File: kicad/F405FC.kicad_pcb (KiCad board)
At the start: 4 copper layers, 36 x 36 mm, 161 parts, among them J1 USB4105-GF-A, J2 ESC, J3 HD VTX, J4 GPS, J5 ELRS, P1 VBAT, P10 LED_DIN, P11 5V, P12 GND, P13 5V, P14 BUZ_N, P15 UART5_TX, P16 UART5_RX, P17 UART6_TX, P18 UART6_RX, P19 MOTOR5, P2 GND, P20 MOTOR6, P21 MOTOR7, P22 MOTOR8, P23 RSSI_IN, P24 GND, P25 5V, P3 10V, P4 GND, P5 CAM1_VID, P6 CAM2_VID, P7 VTX_VID, P8 5V, P9 GND, Q1 PMV40UN2, Q2 NX7002AK, SW1 BOOT, U1 LMR38020FSDDAR, U10 W25N01GV, U11 TS5A3159A, U12 SN74LV1T125, U13 USBLC6-2SC6, U2 LMR38020FSDDAR, U3 STM32F405RGT6, U4 LP38692MP-3.3, U5 LP5907MFX-3.3, U6 ICM-42688-P, U7 BMI270, U8 BMP390, U9 IIS2MDC, Y1 8MHz

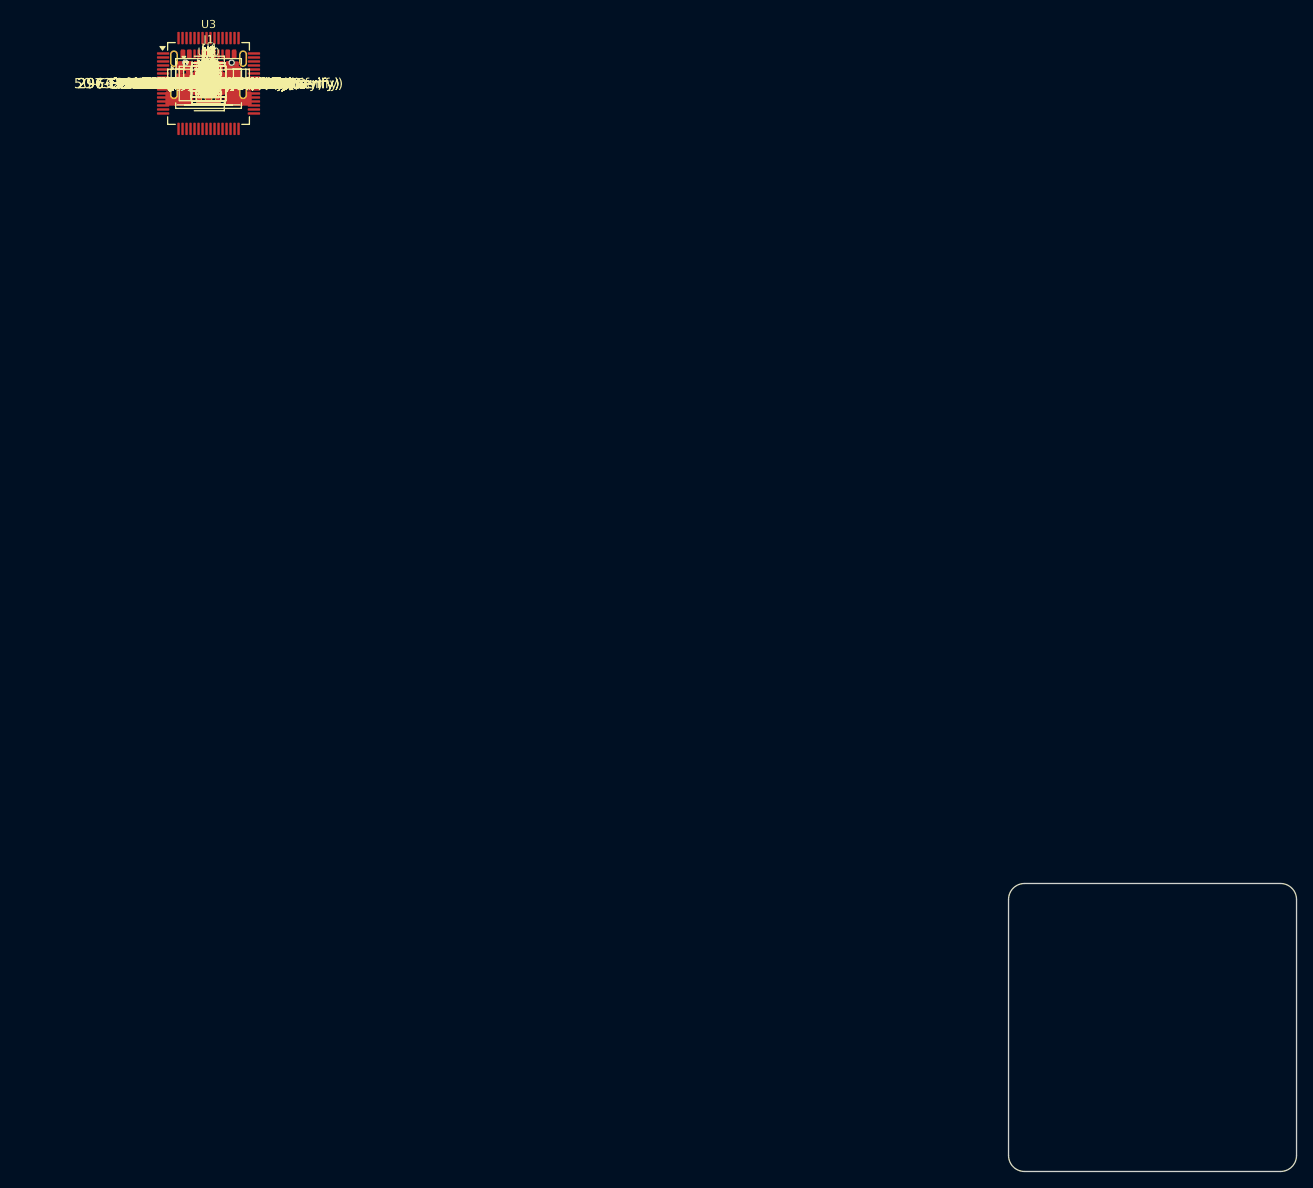
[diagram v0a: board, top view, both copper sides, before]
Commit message: Gate 1 fixes (crystal gm evidence, LDO output ESR, X7R caps, 50V HF cap, per-MPN datasheets, in_bom flags, project-file merge, parity fields), power re-audit fixes (board-level thermal envelope, USB inrush deviation, R41 VTX 0R link), PCB placement + legalizer + grommet keepouts; Gate 1 reports
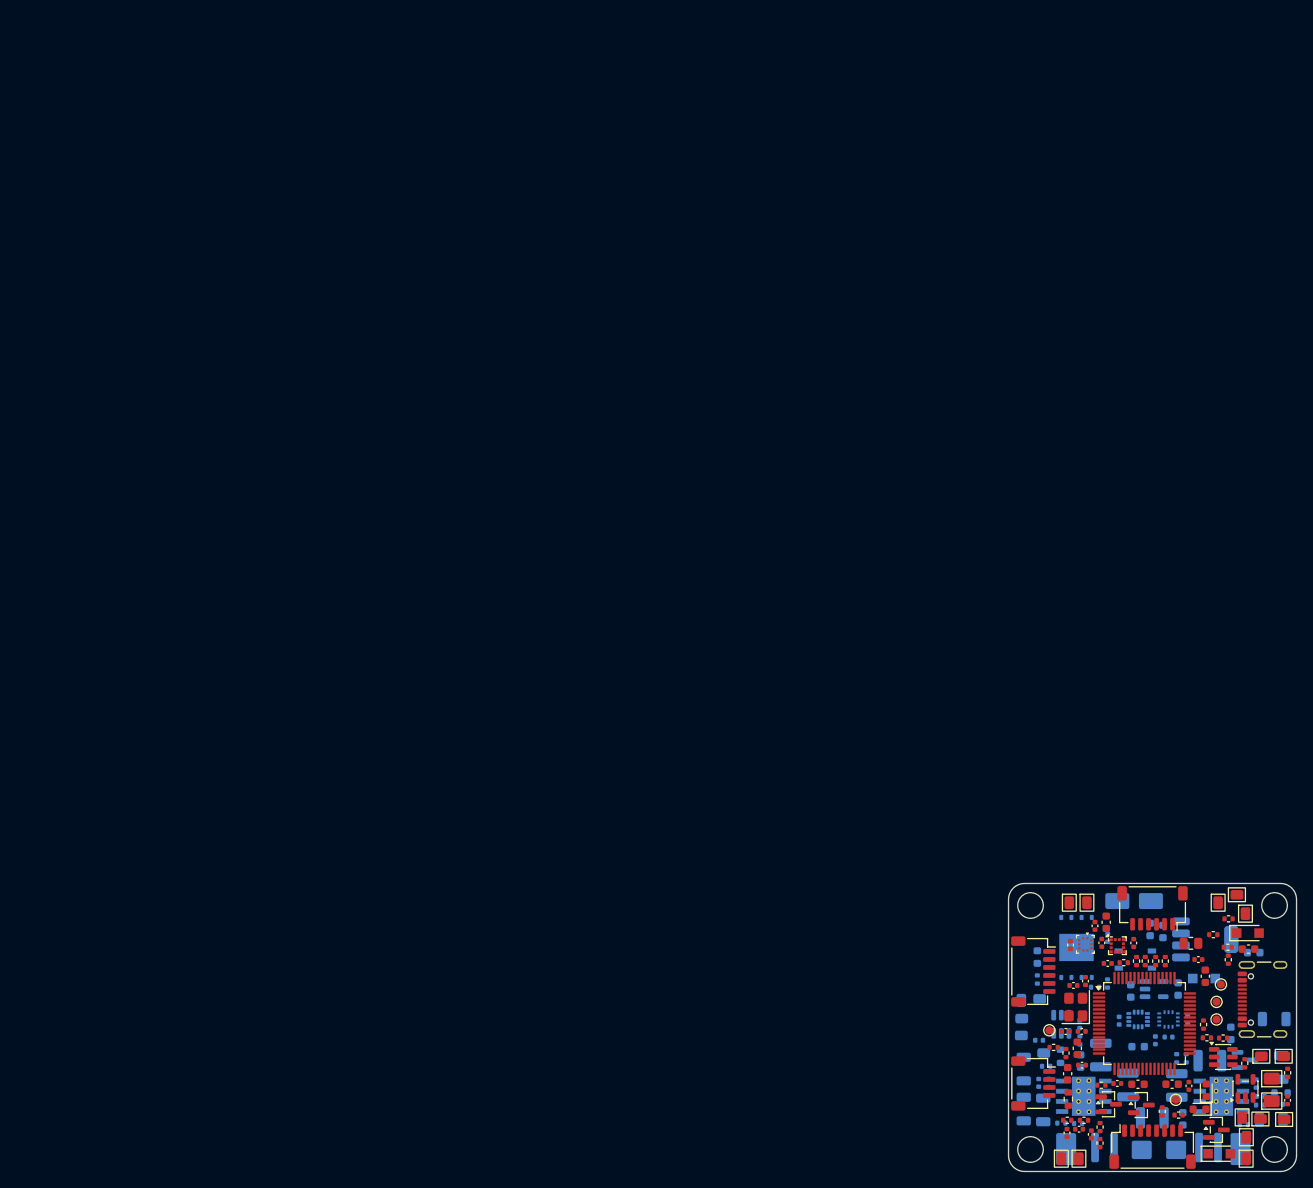
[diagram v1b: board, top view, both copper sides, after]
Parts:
- removed C21: 100nF X7R 16V, Capacitor_SMD:C_0402_1005Metric
- added R41: 0R 2A, Resistor_SMD:R_0805_2012Metric, F.Cu at (122.8, 107.5)
- C1, C10, C11, C12, C13, C14, C15, C16, C19, C2, C22, C3, C38, C4, C40, C41, C42, C48, C49, C5, C6, C7, C8, C9, D1, D10, D5, L1, L2, P1, P2, P3, P4, P5, P6, P7, P8, P9, Q2, R1, R10, R11, R12, R13, R2, R29, R3, R30, R31, R4, R5, R6, R7, R8, R9, SW1, U1, U10, U11, U2, U4, U5, U6, U7: moved to B.Cu
- C17: value 100nF X7R 16V -> 100nF X7R 100V; footprint Capacitor_SMD:C_0402_1005Metric -> Capacitor_SMD:C_0603_1608Metric; moved to B.Cu
- C18: value 4.7uF X5R 10V -> 4.7uF X5R 16V; moved to B.Cu
- C20: value 10uF X5R 25V -> 2.2uF X5R 16V; footprint Capacitor_SMD:C_0805_2012Metric -> Capacitor_SMD:C_0603_1608Metric; moved to B.Cu
- C23, C39: value 2.2uF X5R 16V -> 2.2uF X7R 16V; moved to B.Cu
- C29: value 4.7uF X5R 10V -> 4.7uF X5R 16V
- C47: value 1uF X5R 25V -> 4.7uF X5R 16V
- H1, H2, H3, H4: footprint MountingHole:MountingHole_3.2mm_M3 -> F405FC:MountingHole_3.2mm_M3_Grommet4.6mm
- moved H4 188.4 mm to (133.2, 133.2)
- moved P13 186.8 mm to (129.7, 134.4)
- moved P18 186.7 mm to (134.4, 129.5), turned to 90 degrees
- moved C16 185.5 mm to (132.8, 129.5)
- moved P2 185.4 mm to (129.0, 133.2)
- moved C50 185.3 mm to (134.9, 127.1), turned to 90 degrees
- moved R10 184.9 mm to (133.8, 127.6), turned to 180 degrees
- moved P14 184.9 mm to (129.7, 131.7)
- moved P19 184.5 mm to (131.5, 129.4), turned to 90 degrees
- moved R6 184.1 mm to (134.1, 126.2)
- moved D9 184.0 mm to (126.3, 133.8)
- moved P12 184.0 mm to (132.9, 127.2), turned to 90 degrees
- moved R9 183.5 mm to (129.4, 130.2), turned to 180 degrees
- moved R8 183.3 mm to (131.4, 127.7), turned to 180 degrees
- moved R33 183.0 mm to (134.9, 123.7), turned to 90 degrees
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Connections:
- J3 pad 1: 10V -> VTX_PWR

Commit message: Gate 0 complete (power re-audit round 3 PASS); Gate 1 MCU crystal fix (8.2 pF loads, ECX-32 C0 evidence); net classes; staged board build; routing pipeline; placement renders; raw BOM
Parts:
- C36, C37: value 10pF C0G 50V -> 8.2pF C0G 50V
- moved D5 8.29 mm to (118.2, 106.4)
- moved C18 3.26 mm to (119.8, 109.2)
- moved C19 1.72 mm to (118.8, 104.5), turned to 180 degrees
- moved C20 0.49 mm to (130.2, 108.7)
- moved U4 0.42 mm to (124.3, 107.3), turned to 90 degrees
- moved C22 0.19 mm to (121.2, 113.4)
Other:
- board text added: "10V"
- board text added: "3V3"
- board text added: "5V"
- board text added: "BOOT"
- board text added: "BZ+"
- board text added: "BZ-"
- board text added: "C1"
- board text added: "C2"
- board text added: "CLK"
- board text added: "DIO"
- board text added: "ELRS"
- board text added: "ESC"
- board text added: "G"
- board text added: "GND"
- board text added: "GPS 5V"
- board text added: "LED"
- board text added: "R5"
- board text added: "R6"
- board text added: "RSSI"
- board text added: "RST"
- board text added: "S5"
- board text added: "S6"
- board text added: "S7"
- board text added: "S8"
- board text added: "T5"
- board text added: "T6"
- board text added: "USB"
- board text added: "VBAT"
- board text added: "VID"
- board text added: "VTX 10V"

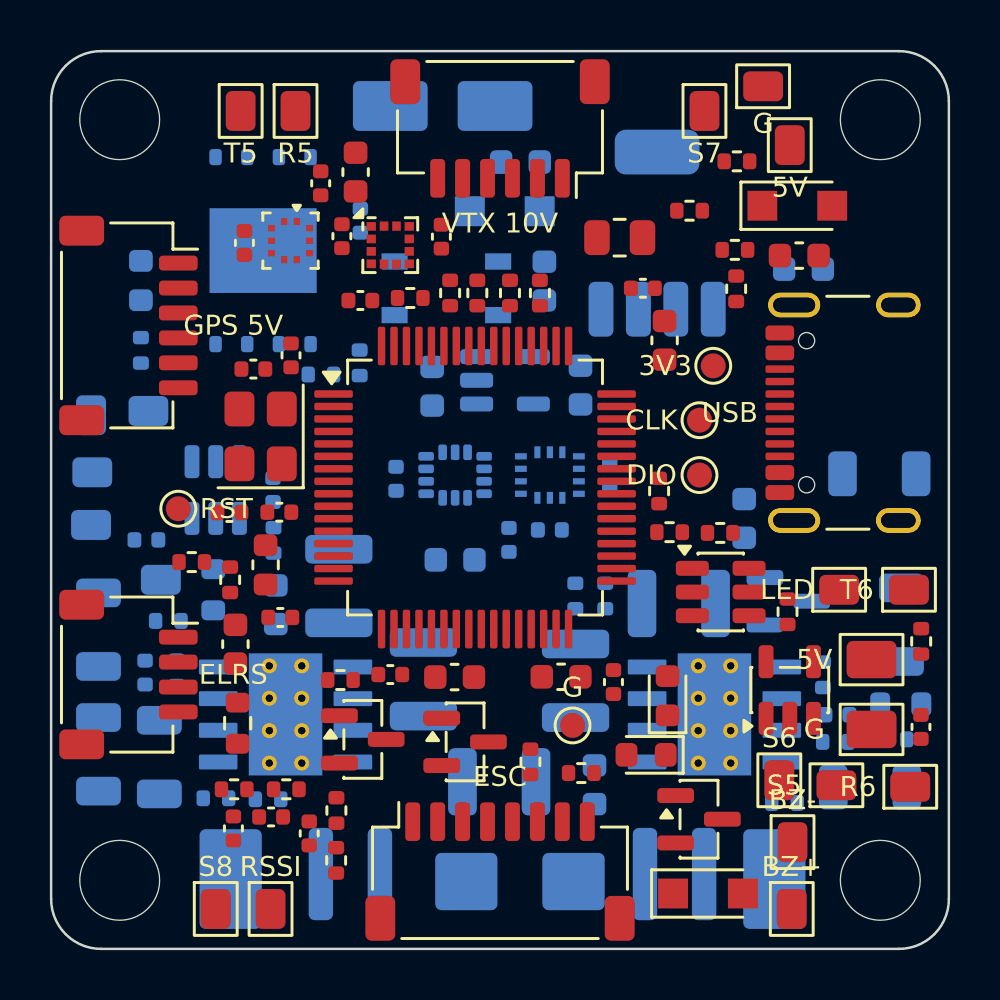
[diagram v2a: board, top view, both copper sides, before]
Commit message: WIP Gate 3 rework: pin-anchored placement, tight legalizer, placecheck; WE-MAPI 4020 inductors, GRM32DR input caps
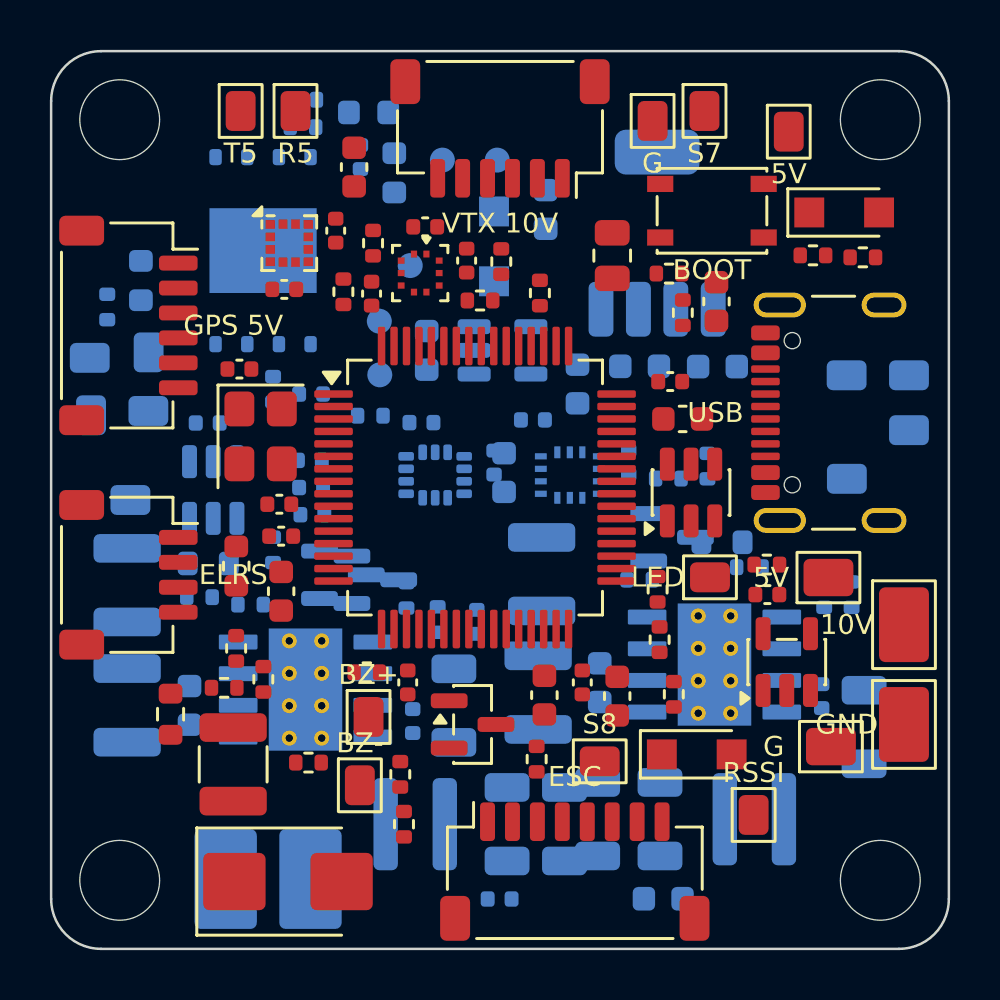
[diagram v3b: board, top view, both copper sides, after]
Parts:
- C1: value 10uF X7R 50V -> 10uF X7R 50V 2.0mm; moved to F.Cu
- C10, C11, C2, C3: value 10uF X7R 50V -> 10uF X7R 50V 2.0mm
- C23, C39: value 2.2uF X7R 16V -> 2.2uF X7R 10V
- C24, C30, C35, C52, C53, D11, D12, D7, D8, P17, P18, P19, P20, R27, R28, TP1, TP2, TP3, TP4, TP5: moved to B.Cu
- D1, P3, P4, SW1: moved to F.Cu
- L1: value 6.8uH -> 5.6uH; footprint Inductor_SMD:L_Wuerth_MAPI-4030 -> Inductor_SMD:L_Wuerth_MAPI-4020
- L2: value 8.2uH -> 5.6uH; footprint Inductor_SMD:L_Wuerth_MAPI-4030 -> Inductor_SMD:L_Wuerth_MAPI-4020
- moved P4 29.7 mm to (134.2, 127.0), turned to 0 degrees
- moved P3 29.3 mm to (134.2, 123.0), turned to 0 degrees
- moved R28 28.2 mm to (110.1, 102.0), turned to 0 degrees
- moved R27 28.2 mm to (110.1, 103.0), turned to 0 degrees
- moved D11 26.3 mm to (112.7, 102.5), turned to 0 degrees
- moved D12 25.4 mm to (113.8, 104.9), turned to 90 degrees
- moved C7 20.2 mm to (120.6, 131.0)
- moved C9 20.2 mm to (118.0, 134.0), turned to 0 degrees
- moved P23 19.7 mm to (128.2, 130.6)
- moved P13 18.6 mm to (112.7, 126.7)
- moved P2 18.6 mm to (110.4, 133.2)
- moved P14 17.5 mm to (112.4, 129.4)
- moved P22 16.5 mm to (122.0, 128.5), turned to 90 degrees
- moved P20 16.5 mm to (131.9, 113.0), turned to 90 degrees
- moved TP1 16.3 mm to (115.7, 104.4)
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
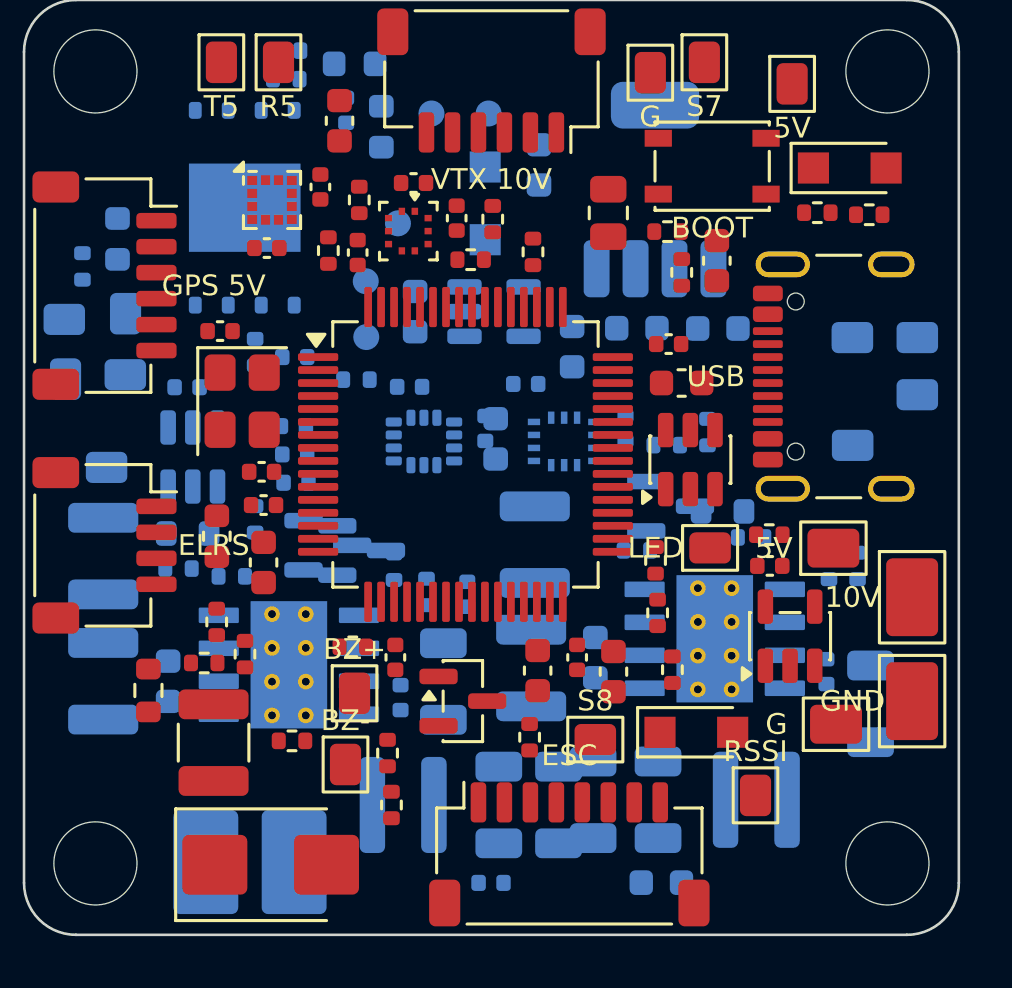
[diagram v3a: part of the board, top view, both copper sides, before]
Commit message: Gate 3 rework: clean placement (0 courtyard/copper DRC, placecheck PASS), 10 V budget 1.3 A with 4020 inductors, D-19
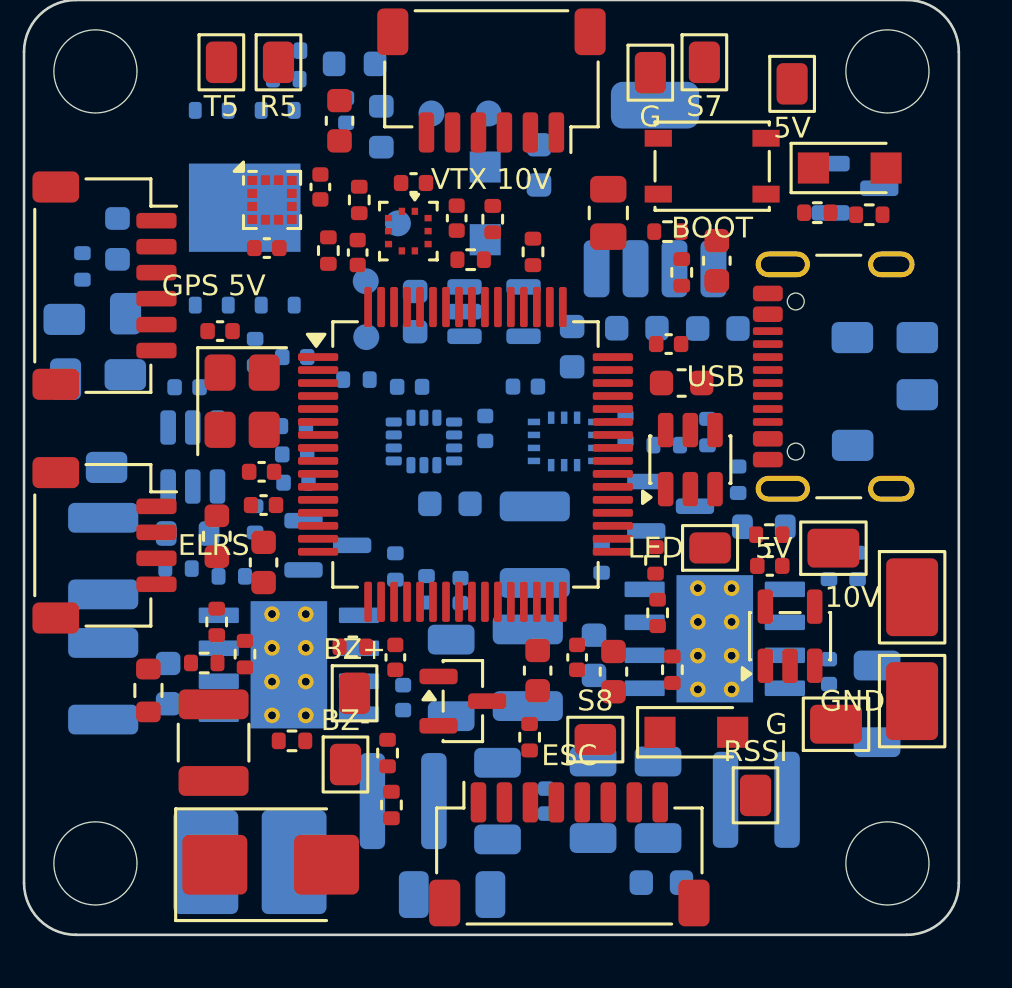
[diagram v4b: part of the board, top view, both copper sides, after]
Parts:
- moved D7 23.6 mm to (132.0, 107.2)
- moved C7 5.36 mm to (116.5, 134.4), turned to 0 degrees
- moved C9 3.80 mm to (120.1, 130.8), turned to 90 degrees
- moved C39 3.06 mm to (116.4, 119.4), turned to 0 degrees
- moved R7 2.28 mm to (127.5, 118.5), turned to 90 degrees
- moved R6 1.70 mm to (128.5, 120.3)
- moved R8 1.40 mm to (122.2, 121.5), turned to 90 degrees
- moved C8 0.33 mm to (116.5, 126.1)
- moved C53 0.30 mm to (116.8, 122.7)
- moved C15 0.25 mm to (132.8, 127.1)
- moved C6 0.16 mm to (118.2, 130.8)
- moved L1 0.15 mm to (114.6, 130.8)
- moved C10 0.13 mm to (119.4, 125.7)
- moved C12 0.10 mm to (122.0, 125.2)
- moved C42 0.10 mm to (119.3, 114.9)
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
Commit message: Gate 2 re-check: report + fixes (TDK 4.7uF 100V bottom input caps, PNs, BOM regenerated $175.73, inductor keepouts), D-20
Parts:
- C1: value 10uF X7R 50V 2.0mm -> 10uF X7R 50V
- C10, C11, C2, C3: value 10uF X7R 50V 2.0mm -> 4.7uF X7S 100V 2.0mm
